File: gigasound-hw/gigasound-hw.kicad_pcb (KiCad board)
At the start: 2 copper layers, 156.1 x 134.5 mm, 132 parts, among them J1 Conn_01x05_Socket_FPC_Joycon, J2 Conn_01x05_Socket_UART, J4 USB_C_Receptacle_USB2.0_16P, J5 PIN_LED_OUT, J6 Conn_01x04_Socket_OLED, SW1 PLAY, SW2 Reset, SW4 STOP, SW5 MODE, U1 STM32F401RETx, U2 USBLC6-2SC6, U5 AMS1117-3.3, Y1 12MHz

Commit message: hw: gigasound logo
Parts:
- added REF**: opensource-logo, gigalibrary:opensource-logo, F.Cu at (187.6, 132.0)
- added REF**: gigasound-logo, gigalibrary:gigasound-logo, F.Cu at (148.7, 142.5)
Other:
- board text added: "https://github.com/Faggenza/gigasound-midi"

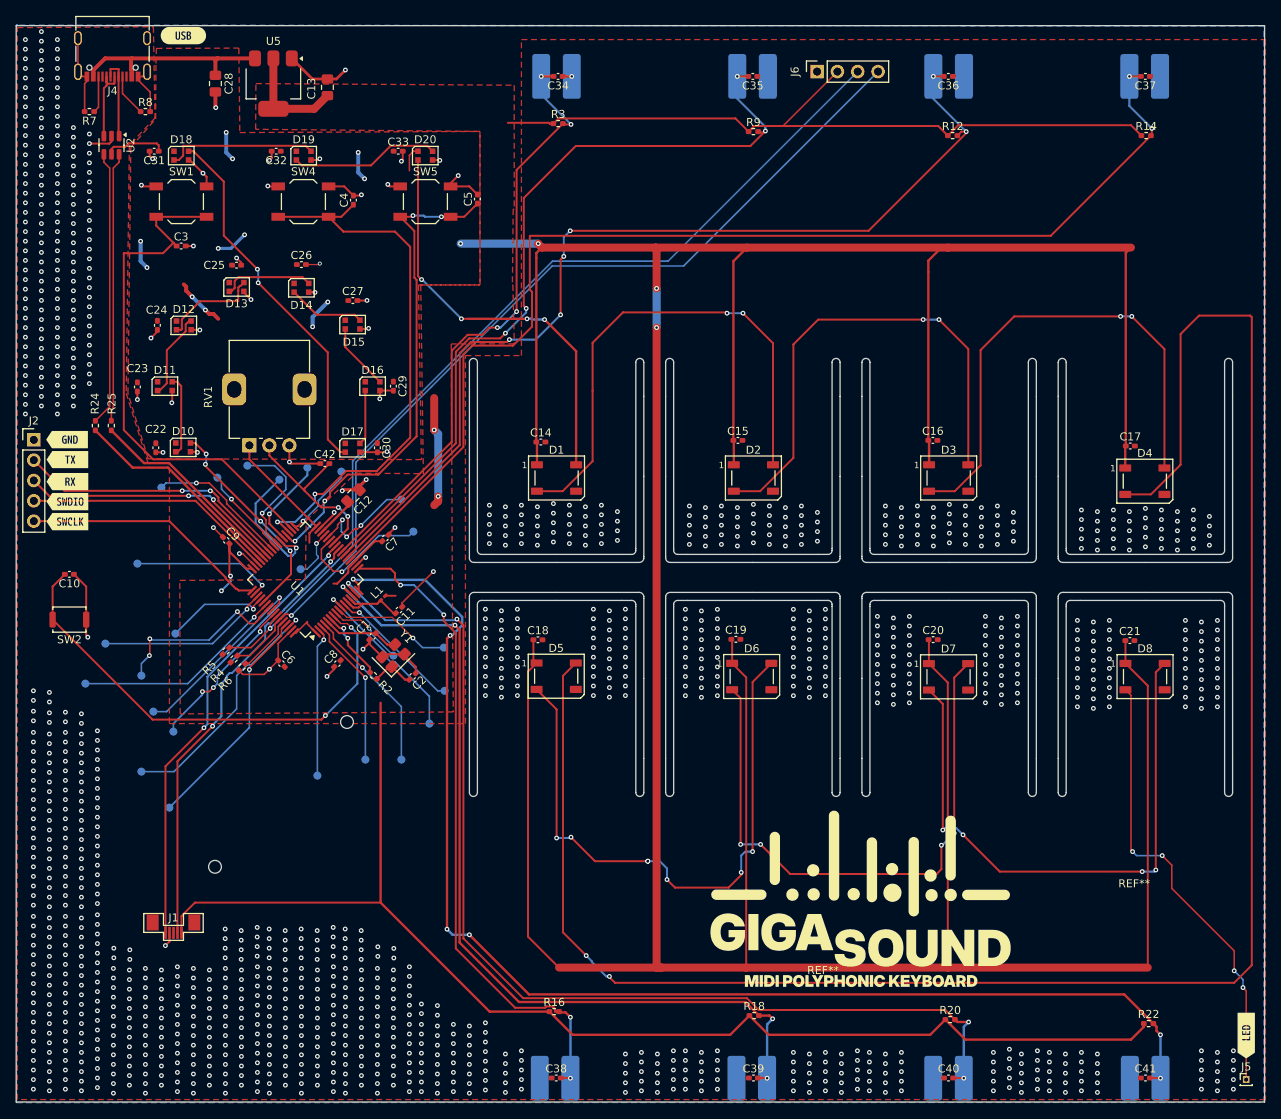
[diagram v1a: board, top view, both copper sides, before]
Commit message: hw: add mounting holes
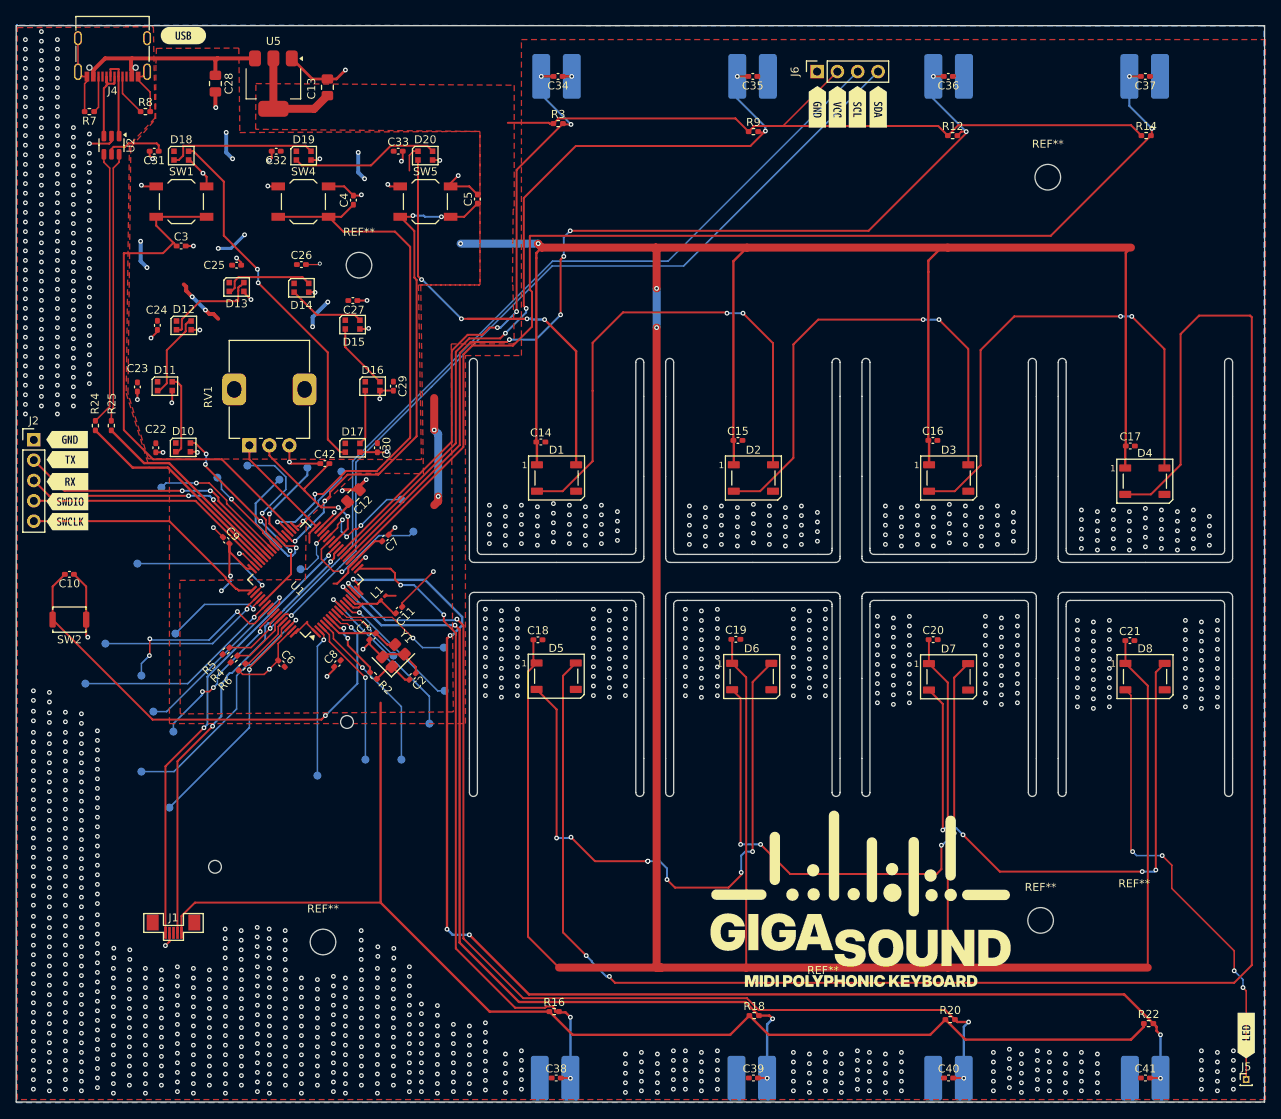
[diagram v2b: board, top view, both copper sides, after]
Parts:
- added REF**: MountingHole_3.2mm_M3, MountingHole:MountingHole_3.2mm_M3, F.Cu at (175.9, 136.1)
- added REF**: MountingHole_3.2mm_M3, MountingHole:MountingHole_3.2mm_M3, F.Cu at (176.8, 43.2)
- added REF**: MountingHole_3.2mm_M3, MountingHole:MountingHole_3.2mm_M3, F.Cu at (90.7, 54.2)
- added REF**: MountingHole_3.2mm_M3, MountingHole:MountingHole_3.2mm_M3, F.Cu at (86.2, 138.8)
- added kibuzzard-682F341C: G***, kibuzzard-682F341C, F.Cu at (148.0, 34.4)
- added kibuzzard-68303C17: G***, kibuzzard-68303C17, F.Cu at (150.5, 34.4)
- added kibuzzard-68303C33: G***, kibuzzard-68303C33, F.Cu at (153.0, 34.4)
- added kibuzzard-68303C3B: G***, kibuzzard-68303C3B, F.Cu at (155.6, 34.4)
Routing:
- net GND: vias 1342 -> 1322
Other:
- board text added: "Rev. 1.0"

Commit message: hw: fix vias on silkscreen
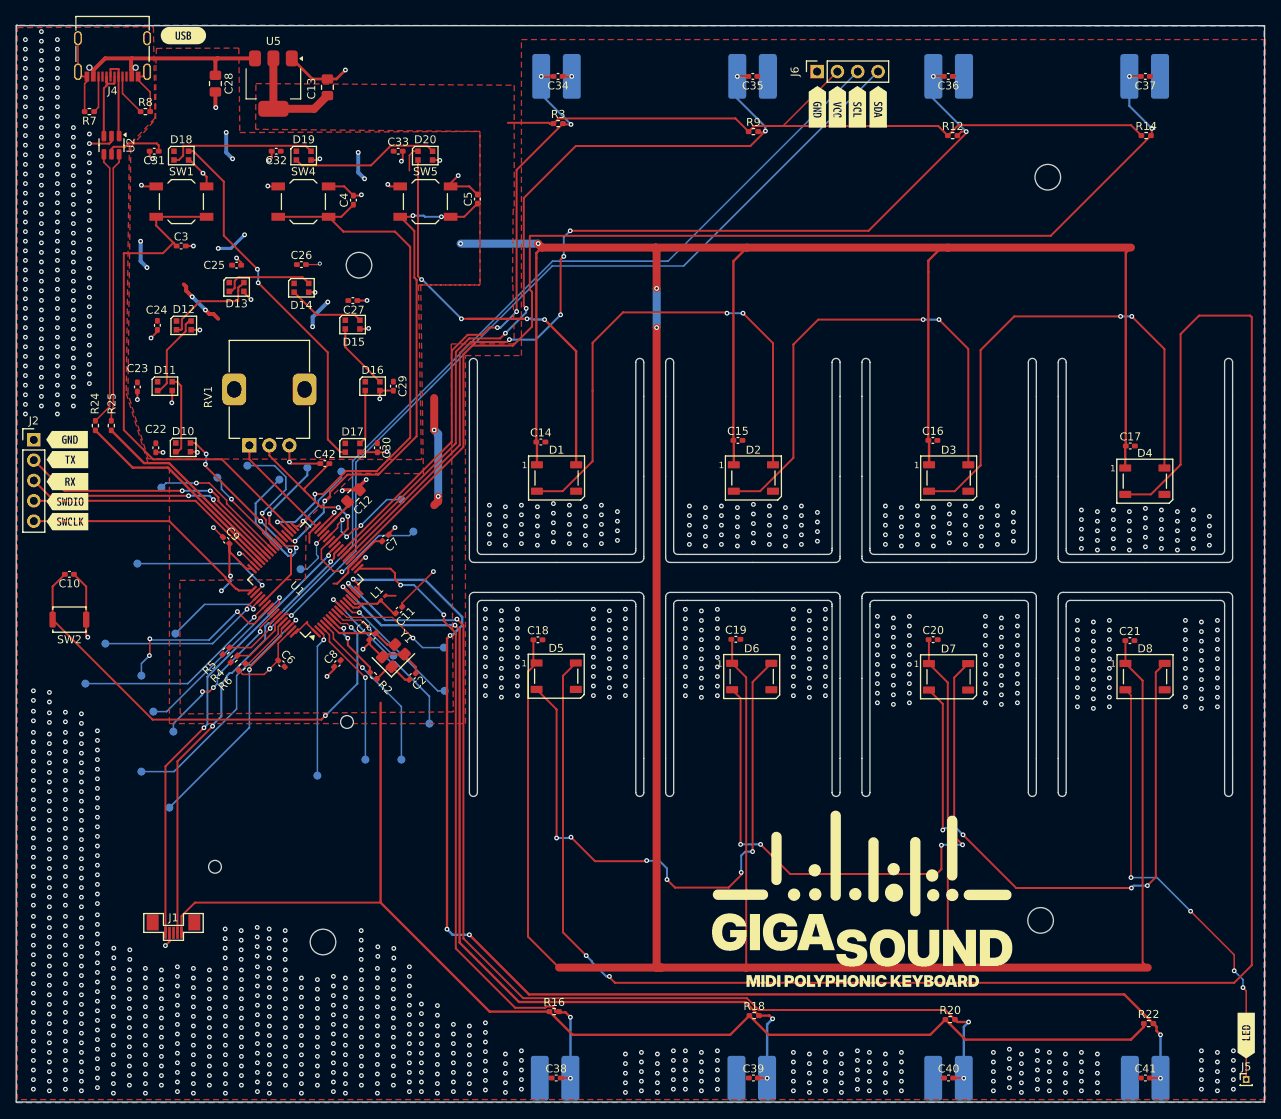
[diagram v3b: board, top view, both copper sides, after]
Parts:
- moved REF** 0.20 mm to (148.9, 142.5)
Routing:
- net Net-(D6-DOUT): track 73.8 -> 76.1 mm
- net Net-(D7-DOUT): track 73.5 -> 75.8 mm
- net Net-(D5-DOUT): vias 7 -> 6

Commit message: hw: final touches
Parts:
- removed kibuzzard-682DE080: G***, kibuzzard-682DE080
- added REF**: MountingHole_3.2mm_M3, MountingHole:MountingHole_3.2mm_M3, F.Cu at (123.8, 43.9)
- added REF**: MountingHole_3.2mm_M3, MountingHole:MountingHole_3.2mm_M3, F.Cu at (122.8, 136.1)
- J5: footprint Connector_PinHeader_1.00mm:PinHeader_1x01_P1.00mm_Vertical -> Connector_PinHeader_2.54mm:PinHeader_1x03_P2.54mm_Vertical
- moved J5 4.80 mm to (201.6, 151.2)
- moved REF** 0.70 mm to (176.8, 43.9)
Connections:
- J5 pad 1: /LED_5050x8/LED_OUT -> 5V
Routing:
- net 5V: track 591.4 -> 607.5 mm, vias 16 -> 17
- net /LED_5050x8/LED_OUT: track 56.8 -> 55.5 mm
- net GND: vias 1322 -> 1317

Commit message: fix clock
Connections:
- U1 pad 12: VDDA -> GND
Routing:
- net GND: track 136.3 -> 145.1 mm
- net VDDA: track 9.15 -> 6.78 mm
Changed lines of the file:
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@@
 			(layers "F.Cu" "F.Mask" "F.Paste")
 			(roundrect_rratio 0.25)
-			(net 9 "VDDA")
+			(net 2 "GND")
 			(pinfunction "VSSA")
 			(pintype "power_in")
@@
 	)
 	(segment
+		(start 93.60586 96.894764)
+		(end 95.087101 98.376005)
+		(width 0.2)
+		(layer "F.Cu")
+		(net 2)
+	)
+	(segment
 		(start 87.875 30.925)
 		(end 89 29.8)
@@
 	)
 	(segment
+		(start 95.417369 98.376005)
+		(end 96.09546 97.697914)
+		(width 0.2)
+		(layer "F.Cu")
+		(net 2)
+	)
+	(segment
 		(start 69.035 51.8)
 		(end 70 51.8)
@@
 	)
 	(segment
+		(start 95.087101 98.376005)
+		(end 95.417369 98.376005)
+		(width 0.2)
+		(layer "F.Cu")
+		(net 2)
+	)
+	(segment
 		(start 93.315 69.87)
 		(end 94.9825 69.87)
@@
 	)
 	(segment
+		(start 96.09546 97.697914)
+		(end 96.09546 96.90454)
+		(width 0.2)
+		(layer "F.Cu")
+		(net 2)
+	)
+	(segment
 		(start 56.6 98.5)
 		(end 56.6 94.375647)
@@
 	)
 	(segment
+		(start 89.869636 96.894764)
+		(end 93.60586 96.894764)
+		(width 0.2)
+		(layer "F.Cu")
+		(net 2)
+	)
+	(segment
 		(start 94.9825 69.87)
 		(end 95 69.8875)
@@
 	)
 	(segment
+		(start 89.250266 96.275394)
+		(end 89.869636 96.894764)
+		(width 0.2)
+		(layer "F.Cu")
+		(net 2)
+	)
+	(segment
 		(start 65.35 44.35)
 		(end 63.65 44.35)
@@
 	)
 	(segment
-		(start 90.658764 96.99)
-		(end 89.964872 96.99)
-		(width 0.25)
-		(layer "F.Cu")
-		(net 9)
-	)
-	(segment
 		(start 93.406031 96.093969)
 		(end 92.981236 96.518764)
@@
 	)
 	(segment
-		(start 89.964872 96.99)
-		(end 89.250266 96.275394)
-		(width 0.25)
-		(layer "F.Cu")
-		(net 9)
-	)
-	(segment
 		(start 95.292894 97.707106)
 		(end 95.019168 97.707106)
@@
 	(segment
 		(start 91.13 96.518764)
-		(end 90.658764 96.99)
-		(width 0.25)
-		(layer "F.Cu")
-		(net 9)
-	)
-	(segment
-		(start 91.13 96.518764)
 		(end 90.200744 96.518764)
 		(width 0.25)
@@
 	)
 	(segment
-		(start 94.856586 98.2162)
+		(start 93.9162 98.2162)
 		(end 89.174404 98.2162)
 		(width 0.15)
@@
 	(segment
 		(start 97.445193 100.804807)
-		(end 94.856586 98.2162)
+		(end 96.504807 100.804807)
+		(width 0.15)
+		(layer "F.Cu")
+		(net 65)
+	)
+	(segment
+		(start 96.504807 100.804807)
+		(end 93.9162 98.2162)
 		(width 0.15)
 		(layer "F.Cu")

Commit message: hw: fix big mistake
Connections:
- C11 pad 1: GND -> VDDA
- C11 pad 2: VDDA -> GND
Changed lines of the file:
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@@
 			(layers "F.Cu" "F.Mask" "F.Paste")
 			(roundrect_rratio 0.25)
-			(net 2 "GND")
+			(net 9 "VDDA")
 			(pintype "passive")
 		)
@@
 			(layers "F.Cu" "F.Mask" "F.Paste")
 			(roundrect_rratio 0.25)
-			(net 9 "VDDA")
+			(net 2 "GND")
 			(pintype "passive")
 		)
